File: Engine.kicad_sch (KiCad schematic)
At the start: 0 parts

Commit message: HUGE TOP LEVEL
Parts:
- added BT?: Battery, symbol Device:Battery
- added F?: 40AFuse, symbol Device:Fuse
- added K?: Starter Relay, symbol SCR23 Library:Relay
- added M?: Starter Motor, symbol Motor:Motor_DC
- added U?: Fuse_Box_Connector, symbol symbols:Fuse_Box_Connector
- added U?: Master Disconnect Switch (Big Red One), symbol symbols:switch
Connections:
- new net: F?.2, K?.30
- new net: K?.87, M?.1 (+)
- new net BAT_FUSE: F?.1
- new net GND: BT?.1 (+), BT?.2 (-), K?.85, M?.2 (-)
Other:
- note added: "DT FUSEBOX Connector"
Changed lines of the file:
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@@
 (kicad_sch (version 20211123) (generator eeschema)
   (paper "A4")
+  (junction (at 207.01 124.46) (diameter 0) (color 0 0 0 0)
+  )
+  (junction (at 207.01 119.38) (diameter 0) (color 0 0 0 0)
+  )
+  (junction (at 153.67 129.54) (diameter 0) (color 0 0 0 0)
+  )
+  (wire (pts (xy 113.03 129.54) (xy 113.03 139.7))
+    (stroke (width 0) (type default) (color 0 0 0 0))
+  )
+  (wire (pts (xy 153.67 119.38) (xy 157.48 119.38))
+    (stroke (width 0) (type default) (color 0 0 0 0))
+  )
+  (wire (pts (xy 168.91 142.24) (xy 209.55 142.24))
+    (stroke (width 0) (type default) (color 0 0 0 0))
+  )
+  (wire (pts (xy 151.13 142.24) (xy 151.13 160.02))
+    (stroke (width 0) (type default) (color 0 0 0 0))
+  )
+  (wire (pts (xy 128.27 129.54) (xy 153.67 129.54))
+    (stroke (width 0) (type default) (color 0 0 0 0))
+  )
+  (wire (pts (xy 165.1 119.38) (xy 207.01 119.38))
+    (stroke (width 0) (type default) (color 0 0 0 0))
+  )
+  (wire (pts (xy 153.67 142.24) (xy 151.13 142.24))
+    (stroke (width 0) (type default) (color 0 0 0 0))
+  )
+  (wire (pts (xy 207.01 124.46) (xy 207.01 119.38))
+    (stroke (width 0) (type default) (color 0 0 0 0))
+  )
+  (wire (pts (xy 95.25 134.62) (xy 95.25 129.54))
+    (stroke (width 0) (type default) (color 0 0 0 0))
+  )
+  (wire (pts (xy 153.67 119.38) (xy 153.67 129.54))
+    (stroke (width 0) (type default) (color 0 0 0 0))
+  )
+  (wire (pts (xy 95.25 129.54) (xy 113.03 129.54))
+    (stroke (width 0) (type default) (color 0 0 0 0))
+  )
+  (wire (pts (xy 207.01 119.38) (xy 212.09 119.38))
+    (stroke (width 0) (type default) (color 0 0 0 0))
+  )
+  (wire (pts (xy 212.09 129.54) (xy 207.01 129.54))
+    (stroke (width 0) (type default) (color 0 0 0 0))
+  )
+  (wire (pts (xy 207.01 129.54) (xy 207.01 124.46))
+    (stroke (width 0) (type default) (color 0 0 0 0))
+  )
+  (wire (pts (xy 207.01 124.46) (xy 212.09 124.46))
+    (stroke (width 0) (type default) (color 0 0 0 0))
+  )
+  (text "DT FUSEBOX\nConnector\n" (at 213.614 125.984 0)
+    (effects (font (size 1.27 1.27)) (justify left bottom))
+  )
+  (label "BAT_FUSE" (at 178.054 119.38 0)
+    (effects (font (size 1.27 1.27)) (justify left bottom))
+  )
+  (symbol (lib_id "Device:Battery") (at 95.25 139.7 0) (unit 1)
+    (in_bom yes) (on_board yes) (fields_autoplaced)
+    (property "Reference" "BT?" (id 0) (at 99.06 138.0489 0)
+      (effects (font (size 1.27 1.27)) (justify left))
+    )
+    (property "Value" "Battery" (id 1) (at 99.06 140.5889 0)
+      (effects (font (size 1.27 1.27)) (justify left))
+    )
+    (property "Footprint" "" (id 2) (at 95.25 138.176 90)
+      (effects (font (size 1.27 1.27)) hide)
+    )
+    (property "Datasheet" "~" (id 3) (at 95.25 138.176 90)
+      (effects (font (size 1.27 1.27)) hide)
+    )
+    (pin "1")
+    (pin "2")
+  )
+  (symbol (lib_id "power:GND") (at 95.25 144.78 0) (unit 1)
+    (in_bom yes) (on_board yes) (fields_autoplaced)
+    (property "Reference" "#PWR?" (id 0) (at 95.25 151.13 0)
+      (effects (font (size 1.27 1.27)) hide)
+    )
+    (property "Value" "GND" (id 1) (at 95.25 149.86 0))
+    (property "Footprint" "" (id 2) (at 95.25 144.78 0)
+      (effects (font (size 1.27 1.27)) hide)
+    )
+    (property "Datasheet" "" (id 3) (at 95.25 144.78 0)
+      (effects (font (size 1.27 1.27)) hide)
+    )
+    (pin "1")
+  )
+  (symbol (lib_id "SCR23 Library:Relay") (at 161.2265 137.2997 180) (unit 1)
+    (in_bom yes) (on_board yes)
+    (property "Reference" "K?" (id 0) (at 161.29 121.158 0)
+      (effects (font (size 1.27 1.27)) hide)
+    )
+    (property "Value" "Starter Relay" (id 1) (at 161.544 149.098 0))
+    (property "Footprint" "" (id 2) (at 127.5715 136.0297 0)
+      (effects (font (size 1.27 1.27)) hide)
+    )
+    (property "Datasheet" "" (id 3) (at 183.8071 135.1915 90)
+      (effects (font (size 1.27 1.27)) hide)
+    )
+    (pin "30")
+    (pin "85")
+    (pin "86")
+    (pin "87")
+  )
+  (symbol (lib_id "power:GND") (at 151.13 160.02 0) (unit 1)
+    (in_bom yes) (on_board yes) (fields_autoplaced)
+    (property "Reference" "#PWR?" (id 0) (at 151.13 166.37 0)
+      (effects (font (size 1.27 1.27)) hide)
+    )
+    (property "Value" "GND" (id 1) (at 151.13 165.1 0))
+    (property "Footprint" "" (id 2) (at 151.13 160.02 0)
+      (effects (font (size 1.27 1.27)) hide)
+    )
+    (property "Datasheet" "" (id 3) (at 151.13 160.02 0)
+      (effects (font (size 1.27 1.27)) hide)
+    )
+    (pin "1")
+  )
+  (symbol (lib_id "Motor:Motor_DC") (at 173.99 132.08 90) (unit 1)
+    (in_bom yes) (on_board yes) (fields_autoplaced)
+    (property "Reference" "M?" (id 0) (at 176.53 123.698 90)
+      (effects (font (size 1.27 1.27)) hide)
+    )
+    (property "Value" "Starter Motor" (id 1) (at 176.53 126.238 90))
+    (property "Footprint" "" (id 2) (at 176.276 132.08 0)
+      (effects (font (size 1.27 1.27)) hide)
+    )
+    (property "Datasheet" "~" (id 3) (at 176.276 132.08 0)
+      (effects (font (size 1.27 1.27)) hide)
+    )
+    (pin "1")
+    (pin "2")
+  )
+  (symbol (lib_id "symbols:Fuse_Box_Connector") (at 219.71 127 270) (unit 1)
+    (in_bom yes) (on_board yes) (fields_autoplaced)
+    (property "Reference" "U?" (id 0) (at 229.87 126.9999 90)
+      (effects (font (size 1.27 1.27)) (justify left) hide)
+    )
+    (property "Value" "Fuse_Box_Connector" (id 1) (at 230.378 128.2699 90)
+      (effects (font (size 1.27 1.27)) (justify left) hide)
+    )
+    (property "Footprint" "" (id 2) (at 219.71 127 0)
+      (effects (font (size 1.27 1.27)) hide)
+    )
+    (property "Datasheet" "" (id 3) (at 219.71 127 0)
+      (effects (font (size 1.27 1.27)) hide)
+    )
+  )
+  (symbol (lib_id "symbols:switch") (at 120.65 129.54 0) (unit 1)
+    (in_bom yes) (on_board yes)
+    (property "Reference" "U?" (id 0) (at 131.318 126.3649 0)
+      (effects (font (size 1.27 1.27)) (justify left) hide)
+    )
+    (property "Value" "Master Disconnect Switch (Big Red One)" (id 1) (at 114.3 132.588 0)
+      (effects (font (size 1.27 1.27)) (justify left))
+    )
+    (property "Footprint" "" (id 2) (at 120.65 129.54 0)
+      (effects (font (size 1.27 1.27)) hide)
+    )
+    (property "Datasheet" "" (id 3) (at 120.65 129.54 0)
+      (effects (font (size 1.27 1.27)) hide)
+    )
+  )
+  (symbol (lib_id "power:GND") (at 113.03 139.7 0) (unit 1)
+    (in_bom yes) (on_board yes)
+    (property "Reference" "#PWR?" (id 0) (at 113.03 146.05 0)
+      (effects (font (size 1.27 1.27)) hide)
+    )
+    (property "Value" "GND" (id 1) (at 113.03 144.78 0))
+    (property "Footprint" "" (id 2) (at 113.03 139.7 0)
+      (effects (font (size 1.27 1.27)) hide)
+    )
+    (property "Datasheet" "" (id 3) (at 113.03 139.7 0)
+      (effects (font (size 1.27 1.27)) hide)
+    )
+    (pin "1")
+  )
+  (symbol (lib_id "power:GND") (at 181.61 132.08 90) (unit 1)
+    (in_bom yes) (on_board yes) (fields_autoplaced)
+    (property "Reference" "#PWR?" (id 0) (at 187.96 132.08 0)
+      (effects (font (size 1.27 1.27)) hide)
+    )
+    (property "Value" "GND" (id 1) (at 185.42 132.0799 90)
+      (effects (font (size 1.27 1.27)) (justify right))
+    )
+    (property "Footprint" "" (id 2) (at 181.61 132.08 0)
+      (effects (font (size 1.27 1.27)) hide)
+    )
+    (property "Datasheet" "" (id 3) (at 181.61 132.08 0)
+      (effects (font (size 1.27 1.27)) hide)
+    )
+    (pin "1")
+  )
+  (symbol (lib_id "Device:Fuse") (at 161.29 119.38 270) (unit 1)
+    (in_bom yes) (on_board yes) (fields_autoplaced)
+    (property "Reference" "F?" (id 0) (at 161.29 113.03 90)
+      (effects (font (size 1.27 1.27)) hide)
+    )
+    (property "Value" "40AFuse" (id 1) (at 161.29 115.57 90))
+    (property "Footprint" "" (id 2) (at 161.29 117.602 90)
+      (effects (font (size 1.27 1.27)) hide)
+    )
+    (property "Datasheet" "~" (id 3) (at 161.29 119.38 0)
+      (effects (font (size 1.27 1.27)) hide)
+    )
+    (pin "1")
+    (pin "2")
+  )
 )

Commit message: Filled in Many Sheets
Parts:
- added L?: COIL 3, symbol Device:L
- added L?: COIL 4, symbol Device:L
- added L?: COIL 1, symbol Device:L
- added L?: COIL 2, symbol Device:L
- added U?: INJECTOR 4, symbol SCR23 Library:Injector
- added U?: DT_12P_Green_Male, symbol SCR23 Library:DT_12_Pin
- added U?: INJECTOR 1, symbol SCR23 Library:Injector
- added U?: DTM_12P_Green_Male, symbol SCR23 Library:DT_12_Pin
- added U?: INJECTOR 2, symbol SCR23 Library:Injector
- added U?: INJECTOR 3, symbol SCR23 Library:Injector
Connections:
- new net COIL_1: L?.1
- new net COIL_2: L?.1
- new net COIL_3: L?.1
- new net COIL_4: L?.1
- new net COIL_POWER: L?.2, L?.2, L?.2, L?.2
- new net INJECTOR_POWER: U?., U?., U?., U?.
- new net INJ_1: U?.
- new net INJ_2: U?.
- new net INJ_3: U?.
- new net INJ_4: U?.
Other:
- note added: "DT 12P BROWN MALE"
- note added: "Starter Motor Overview"
- note removed: "DT FUSEBOX Connector"
- moved on the sheet: BT?

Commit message: Updated Connectors
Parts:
- U?: Part # (none) -> AT04-12PC-SR2GN
- U?: Part # (none) -> ATM04-12PC-SR1GN
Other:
- note added: "ENGINE to ECU"
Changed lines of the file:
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@@
     (stroke (width 0) (type default) (color 0 0 0 0))
   )
+  (text "ENGINE to ECU" (at 113.03 25.4 0)
+    (effects (font (size 1.27 1.27)) (justify left bottom))
+  )
   (text "Starter Motor Overview" (at 26.67 139.954 0)
+    (effects (font (size 1.27 1.27)) (justify left bottom))
+  )
+  (text "ENGINE to ECU" (at 193.802 25.654 0)
     (effects (font (size 1.27 1.27)) (justify left bottom))
   )
@@
   )
   (symbol (lib_id "SCR23 Library:DT_12_Pin") (at 119.888 42.164 0) (unit 1)
-    (in_bom yes) (on_board yes) (fields_autoplaced)
+    (in_bom yes) (on_board yes)
     (property "Reference" "U?" (id 0) (at 120.2055 24.892 0)
       (effects (font (size 1.27 1.27)) hide)
@@
       (effects (font (size 1.27 1.27)) hide)
     )
+    (property "Part #" "AT04-12PC-SR2GN" (id 4) (at 119.888 55.118 0))
     (pin "1")
     (pin "10")
@@
   )
   (symbol (lib_id "SCR23 Library:DT_12_Pin") (at 200.66 42.164 0) (unit 1)
-    (in_bom yes) (on_board yes) (fields_autoplaced)
+    (in_bom yes) (on_board yes)
     (property "Reference" "U?" (id 0) (at 200.9775 24.892 0)
       (effects (font (size 1.27 1.27)) hide)
@@
       (effects (font (size 1.27 1.27)) hide)
     )
+    (property "Part #" "ATM04-12PC-SR1GN" (id 4) (at 200.914 54.864 0))
     (pin "1")
     (pin "10")

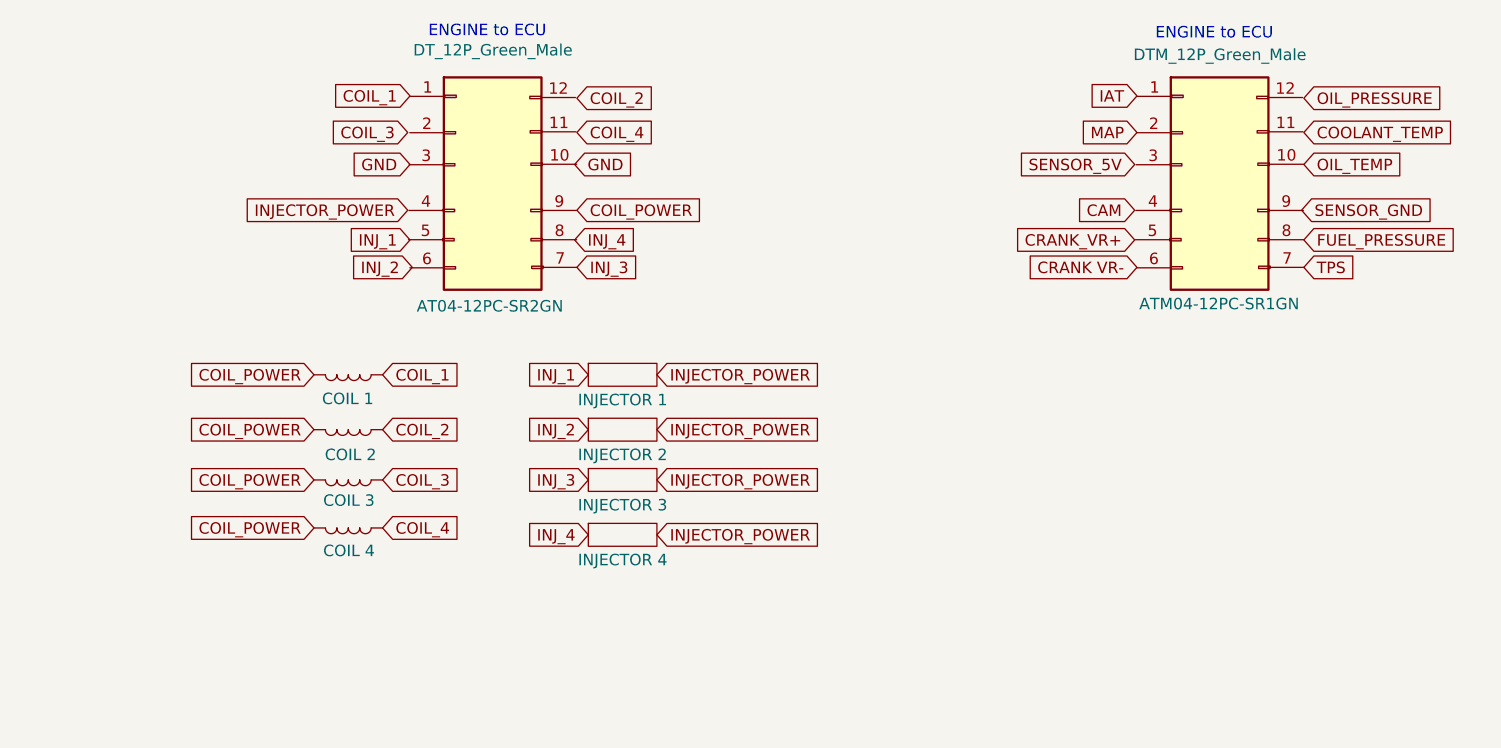
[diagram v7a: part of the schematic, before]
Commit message: Connector Numbers 1
Added Numbers to all of the connectors that were numbered and in KiCad so far
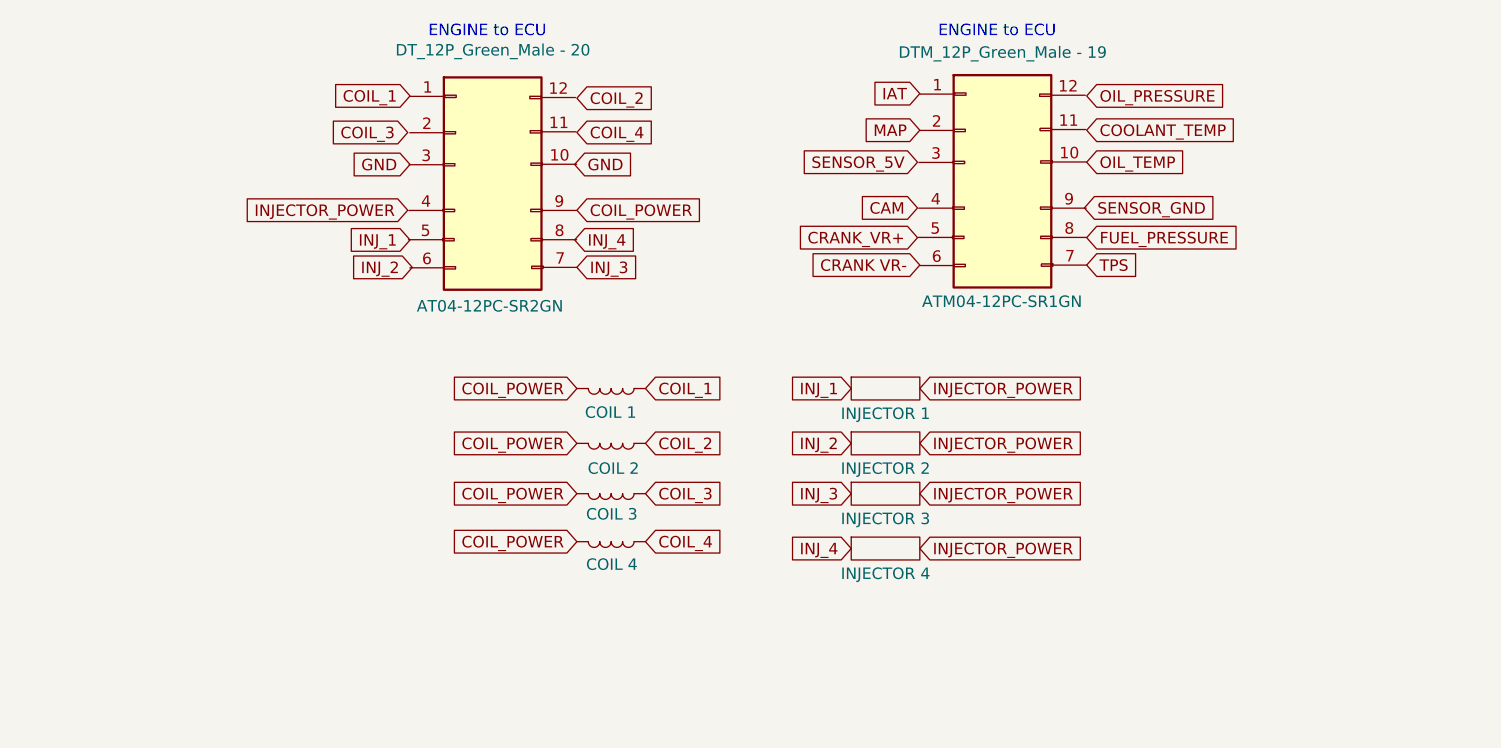
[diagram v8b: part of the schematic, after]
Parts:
- U?: value DT_12P_Green_Male -> DT_12P_Green_Male - 20
- U?: value DTM_12P_Green_Male -> DTM_12P_Green_Male - 19
